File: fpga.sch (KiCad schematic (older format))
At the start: 27 parts, among them IC1 EP4CE10F17, J1 Pinheader_2x5_TH_WALL, U21 EPCS4

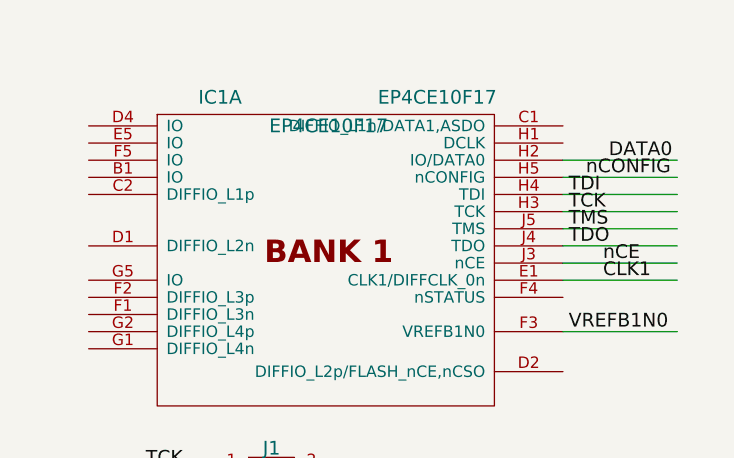
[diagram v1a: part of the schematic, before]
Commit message: Added VCCINT power supply
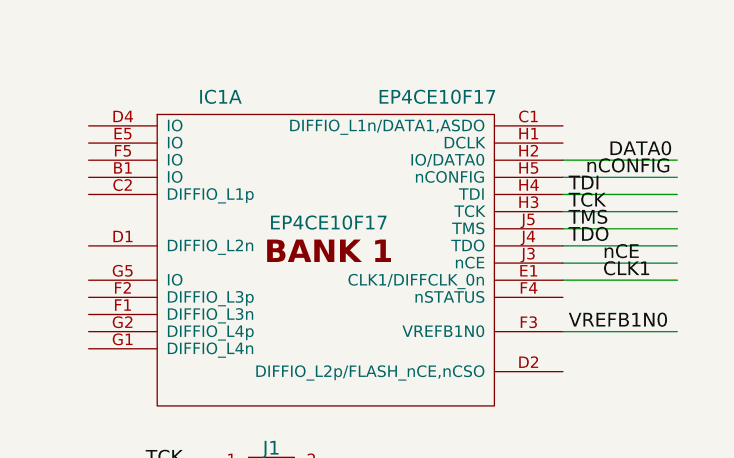
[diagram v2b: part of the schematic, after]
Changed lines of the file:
@@
 EESchema Schematic File Version 2
-LIBS:Sputnik-rescue
 LIBS:sputnik
 LIBS:power
@@
 LIBS:Winbond
 LIBS:Sputnik-cache
-EELAYER 26 0
+EELAYER 25 0
 EELAYER END
 $Descr A3 16535 11693
@@
 P 2600 2125
 F 0 "IC1" H 2125 3400 60  0000 C CNN
-F 1 "EP4CE10F17" H 2600 3275 60  0000 C CNN
+F 1 "EP4CE10F17" H 2600 2850 60  0000 C CNN
 F 2 "lib:BGA-256-NSMD" H 2600 3700 60  0001 C CNN
 F 3 "" H 500 75  60  0000 C CNN
@@
 $EndComp
 $Comp
-L GND #PWR10
+L GND #PWR6
 U 1 1 5807C448
 P 12075 6725
-F 0 "#PWR10" H 12075 6475 50  0001 C CNN
+F 0 "#PWR6" H 12075 6475 50  0001 C CNN
 F 1 "GND" H 12075 6575 50  0000 C CNN
 F 2 "" H 12075 6725 50  0000 C CNN
@@
 $EndComp
 $Comp
-L GND #PWR4
+L GND #PWR5
 U 1 1 57F7A288
 P 2675 3000
-F 0 "#PWR4" H 2675 2750 50  0001 C CNN
+F 0 "#PWR5" H 2675 2750 50  0001 C CNN
 F 1 "GND" H 2675 2850 50  0000 C CNN
 F 2 "" H 2675 3000 50  0000 C CNN
@@
 NoConn ~ 2600 2775
 $Comp
-L +3V3 #PWR2
+L +3V3 #PWR8
 U 1 1 57F8D5C6
 P 13775 2025
-F 0 "#PWR2" H 13875 2075 20  0001 C CNN
+F 0 "#PWR8" H 13875 2075 20  0001 C CNN
 F 1 "+3V3" H 13775 2115 30  0000 C CNN
 F 2 "" H 13775 2025 60  0000 C CNN
@@
 $EndComp
 $Comp
-L GND #PWR3
+L GND #PWR9
 U 1 1 57F8FD8F
 P 13775 2325
-F 0 "#PWR3" H 13775 2075 50  0001 C CNN
+F 0 "#PWR9" H 13775 2075 50  0001 C CNN
 F 1 "GND" H 13775 2175 50  0000 C CNN
 F 2 "" H 13775 2325 50  0000 C CNN
@@
 $EndComp
 $Comp
-L GND #PWR1
+L GND #PWR7
 U 1 1 57F90743
 P 13275 1400
-F 0 "#PWR1" H 13275 1150 50  0001 C CNN
+F 0 "#PWR7" H 13275 1150 50  0001 C CNN
 F 1 "GND" H 13275 1250 50  0000 C CNN
 F 2 "" H 13275 1400 50  0000 C CNN
@@
 $EndComp
 $Comp
-L GND #PWR8
+L GND #PWR2
 U 1 1 58612A86
 P 1700 4125
-F 0 "#PWR8" H 1700 3875 50  0001 C CNN
+F 0 "#PWR2" H 1700 3875 50  0001 C CNN
 F 1 "GND" H 1700 3975 50  0000 C CNN
 F 2 "" H 1700 4125 50  0000 C CNN
@@
 $EndComp
 $Comp
-L +3V3 #PWR5
+L +3V3 #PWR3
 U 1 1 586140D5
 P 2650 3775
-F 0 "#PWR5" H 2750 3825 20  0001 C CNN
+F 0 "#PWR3" H 2750 3825 20  0001 C CNN
 F 1 "+3V3" H 2650 3865 30  0000 C CNN
 F 2 "" H 2650 3775 60  0000 C CNN
@@
 Connection ~ 2650 3825
 $Comp
-L +3V3 #PWR7
+L +3V3 #PWR1
 U 1 1 58614C3F
 P 1575 4025
-F 0 "#PWR7" H 1675 4075 20  0001 C CNN
+F 0 "#PWR1" H 1675 4075 20  0001 C CNN
 F 1 "+3V3" H 1575 4115 30  0000 C CNN
 F 2 "" H 1575 4025 60  0000 C CNN
@@
 $EndComp
 $Comp
-L GND #PWR9
+L GND #PWR4
 U 1 1 586161B6
 P 2650 4500
-F 0 "#PWR9" H 2650 4250 50  0001 C CNN
+F 0 "#PWR4" H 2650 4250 50  0001 C CNN
 F 1 "GND" H 2650 4350 50  0000 C CNN
 F 2 "" H 2650 4500 50  0000 C CNN
@@
 $EndComp
 $Comp
-L GND #PWR6
+L GND #PWR10
 U 1 1 5883481A
 P 14050 3950
-F 0 "#PWR6" H 14050 3700 50  0001 C CNN
+F 0 "#PWR10" H 14050 3700 50  0001 C CNN
 F 1 "GND" H 14050 3800 50  0000 C CNN
 F 2 "" H 14050 3950 50  0000 C CNN

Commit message: Up
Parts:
- added C127: 0,01, Capacitors_SMD:C_0603, symbol C
- added C128: TBD, Capacitors_SMD:C_0603, symbol C
- added Y3: Crystal_GND24, symbol Crystal_GND24
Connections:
- net labels added: CLK50
- net labels removed: CLK1, VCCA2
- wire segments 155 -> 120
- no-connect marks 3 -> 4

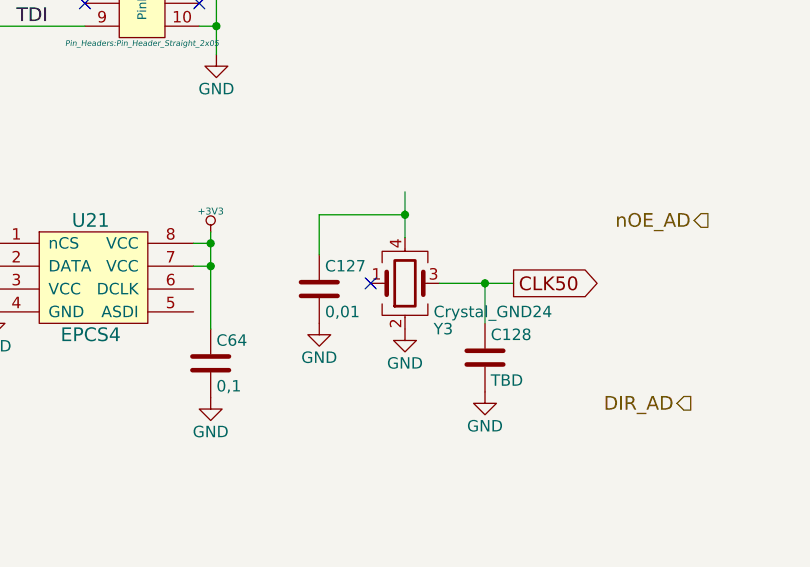
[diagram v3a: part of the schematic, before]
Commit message: Add KXO-V97 footprint
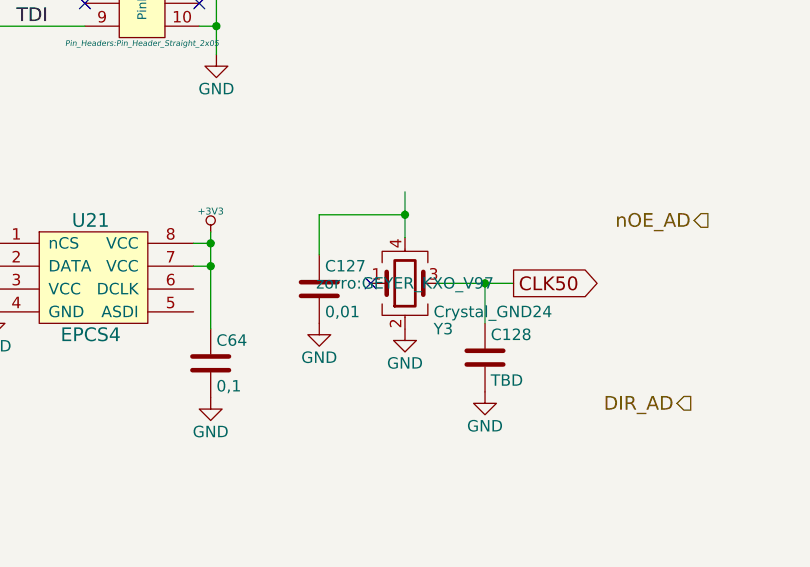
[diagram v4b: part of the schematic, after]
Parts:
- Y3: footprint (none) -> zorro:GEYER_KXO_V97
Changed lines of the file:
@@
 F 0 "Y3" H 3625 4200 50  0000 L CNN
 F 1 "Crystal_GND24" H 3625 4125 50  0000 L CNN
-F 2 "" H 3500 4000 50  0000 C CNN
+F 2 "zorro:GEYER_KXO_V97" H 3500 4000 50  0000 C CNN
 F 3 "" H 3500 4000 50  0000 C CNN
 	1    3500 4000

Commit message: A bit of update
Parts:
- added R34, R35, R36: 10K, Resistors_SMD:R_0603, symbol R_Small
- added R37: 25, Resistors_SMD:R_0603, symbol R_Small
- added R38: 000, Resistors_SMD:R_0603, symbol R_Small
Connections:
- net labels added: ASDO, CONF_DONE, DCLK, nCSO, nSTATUS
- net labels removed: VCCIO1
- wire segments 120 -> 136
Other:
- note added: "ABRACON ASE-50"
- moved on the sheet: C127, C128, Y3

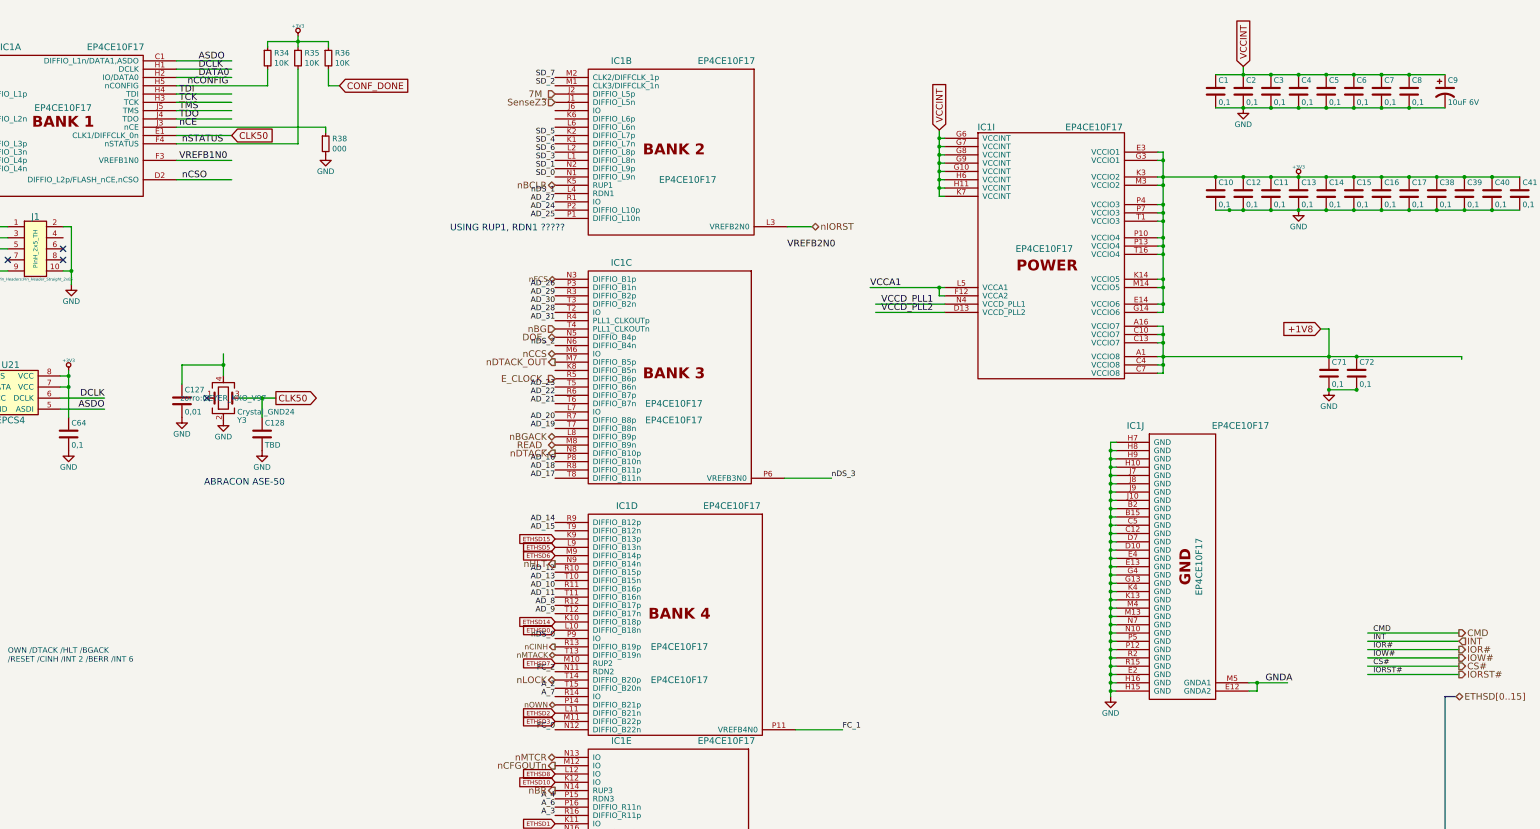
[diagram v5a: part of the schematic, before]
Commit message: VCCA and VCCD_PLL
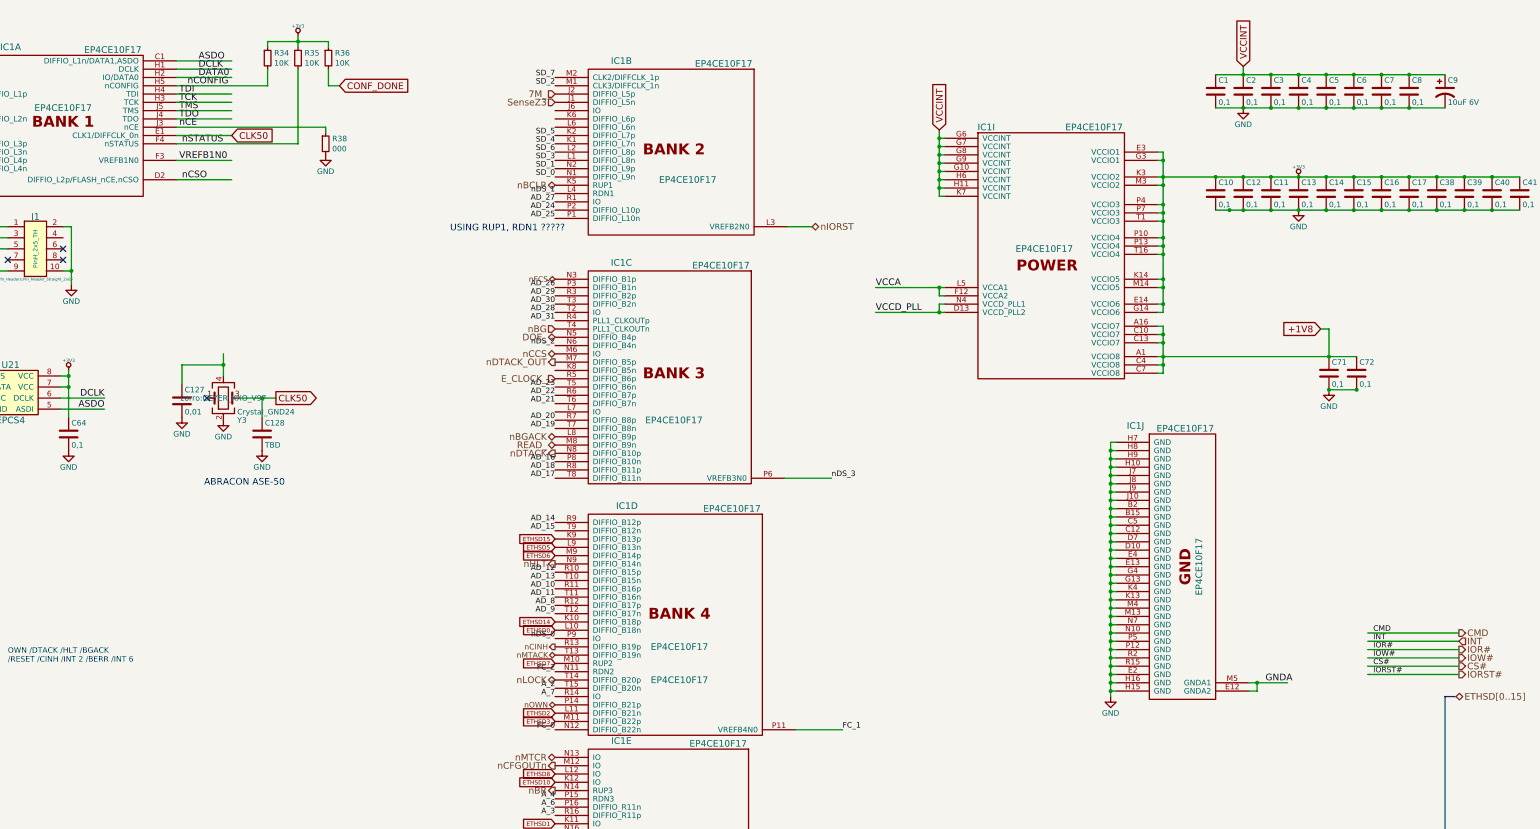
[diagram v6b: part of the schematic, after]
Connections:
- net labels added: VCCA, VCCD_PLL
- net labels removed: VCCA1, VCCD_PLL1, VCCD_PLL2, VREFB2N0
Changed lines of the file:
@@
 F 2 "lib:BGA-256-NSMD" H 2600 3700 60  0001 C CNN
 F 3 "" H 500 75  60  0000 C CNN
-F 4 "EP4CE10F17" H 3075 3400 60  0000 C CNN "Component Value"
+F 4 "EP4CE10F17" H 3050 3375 60  0000 C CNN "Component Value"
 	1    2600 2125
 	1    0    0    -1
@@
 F 2 "lib:BGA-256-NSMD" H 8125 3825 60  0001 C CNN
 F 3 "" H 6025 200 60  0000 C CNN
-F 4 "EP4CE10F17" H 8600 3525 60  0000 C CNN "Component Value"
+F 4 "EP4CE10F17" H 8575 3500 60  0000 C CNN "Component Value"
 	2    8125 2250
 	1    0    0    -1
@@
 F 2 "lib:BGA-256-NSMD" H 8125 5650 60  0001 C CNN
 F 3 "" H 6025 2025 60  0000 C CNN
-F 4 "EP4CE10F17" H 8125 4075 60  0000 C CNN "Component Value"
+F 4 "EP4CE10F17" H 8550 5325 60  0000 C CNN "Component Value"
 	3    8125 4075
 	1    0    0    -1
@@
 F 2 "lib:BGA-256-NSMD" H 12775 7125 60  0001 C CNN
 F 3 "" H 10675 3500 60  0000 C CNN
-F 4 "EP4CE10F17" H 13250 6825 60  0000 C CNN "Component Value"
+F 4 "EP4CE10F17" H 12750 6800 60  0000 C CNN "Component Value"
 	10   12775 5550
 	1    0    0    -1
@@
 Text GLabel 10525 1600 1    60   Input ~ 0
 VCCINT
-Text Label 9900 3025 0    60   ~ 0
-VCCA1
-Text Label 10000 3175 0    60   ~ 0
-VCCD_PLL1
-Text Label 10000 3250 0    60   ~ 0
-VCCD_PLL2
+Text Label 9950 3025 0    60   ~ 0
+VCCA
+Text Label 9950 3250 0    60   ~ 0
+VCCD_PLL
 Text Label 3650 1875 0    60   ~ 0
 VREFB1N0
@@
 F 2 "lib:BGA-256-NSMD" H 8175 7850 60  0001 C CNN
 F 3 "" H 6075 4225 60  0000 C CNN
-F 4 "EP4CE10F17" H 8650 7550 60  0000 C CNN "Component Value"
+F 4 "EP4CE10F17" H 8650 7525 60  0000 C CNN "Component Value"
 	4    8175 6275
 	1    0    0    -1
@@
 	1    0    0    -1
 $EndComp
-Text Label 9150 2675 0    60   ~ 0
-VREFB2N0
 $Comp
 L C C10
@@
 F 2 "lib:BGA-256-NSMD" H 8125 9975 60  0001 C CNN
 F 3 "" H 6025 6350 60  0000 C CNN
-F 4 "EP4CE10F17" H 8600 9675 60  0000 C CNN "Component Value"
+F 4 "EP4CE10F17" H 8525 9650 60  0000 C CNN "Component Value"
 	5    8125 8400
 	1    0    0    -1
@@
 	12550 1875 12500 1875
 Wire Wire Line
-	12500 2100 12550 2100
+	12550 2100 12500 2100
 Wire Wire Line
 	12550 1800 12550 3250
@@
 Connection ~ 12550 3175
 Wire Wire Line
-	12500 3650 15250 3650
+	12500 3650 14300 3650
 Wire Wire Line
 	12550 3525 12500 3525
@@
 Connection ~ 12550 3725
 Wire Wire Line
-	9900 3025 10575 3025
+	9950 3025 10575 3025
 Wire Wire Line
 	10525 3100 10575 3100
 Wire Wire Line
-	10575 3175 9950 3175
-Wire Wire Line
-	10575 3250 9950 3250
+	10575 3175 10525 3175
+Wire Wire Line
+	9950 3250 10575 3250
 Wire Wire Line
 	3625 1125 4125 1125
@@
 	1    0    0    -1
 $EndComp
-Wire Wire Line
-	15250 3650 15250 3675
 Connection ~ 14050 3650
 Text GLabel 13975 3400 0    60   Input ~ 0
@@
 Connection ~ 14050 3950
 Connection ~ 14300 3950
-Connection ~ 14300 3650
 Text HLabel 15100 8275 2    60   BiDi ~ 0
 USBAD[0:15]
@@
 Connection ~ 12550 1875
 $Comp
-L +3V3 #PWR?
+L +3V3 #PWR015
 U 1 1 58AD9DC7
 P 4725 750
-F 0 "#PWR?" H 4825 800 20  0001 C CNN
+F 0 "#PWR015" H 4825 800 20  0001 C CNN
 F 1 "+3V3" H 4725 840 30  0000 C CNN
 F 2 "" H 4725 750 60  0000 C CNN
@@
 	4725 750  4725 850
 Connection ~ 4725 800
+Wire Wire Line
+	10525 3175 10525 3250
+Connection ~ 10525 3250
 $EndSCHEMATC

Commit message: VCCA added
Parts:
- added R45: 000, Resistors_SMD:R_0603, symbol R_Small
- Y3: footprint zorro:GEYER_KXO_V97 -> Crystals:Crystal_SMD_3225-4pin_3.2x2.5mm
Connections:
- net labels added: +2V5
- net labels removed: VCCA
- wire segments 136 -> 139
- no-connect marks 4 -> 3
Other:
- note added: "ABRACON ASE-50 (3.3V)\nASE2 (2.5V)"
- note removed: "ABRACON ASE-50"
- moved on the sheet: C127, C128
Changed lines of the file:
@@
 EESchema Schematic File Version 2
-LIBS:Sputnik-rescue
 LIBS:sputnik
 LIBS:power
@@
 LIBS:Winbond
 LIBS:Sputnik-cache
-EELAYER 26 0
+EELAYER 25 0
 EELAYER END
 $Descr A3 16535 11693
@@
 Text GLabel 10525 1600 1    60   Input ~ 0
 VCCINT
-Text Label 9950 3025 0    60   ~ 0
-VCCA
 Text Label 9950 3250 0    60   ~ 0
 VCCD_PLL
@@
 F 0 "Y3" H 4175 4225 50  0000 L CNN
 F 1 "Crystal_GND24" H 4175 4150 50  0000 L CNN
-F 2 "zorro:GEYER_KXO_V97" H 4050 4025 50  0000 C CNN
+F 2 "Crystals:Crystal_SMD_3225-4pin_3.2x2.5mm" H 4050 4450 50  0000 C CNN
 F 3 "" H 4050 4025 50  0000 C CNN
 	1    4050 4025
@@
 	1    0    0    -1
 $EndComp
-NoConn ~ 3900 4025
-Wire Wire Line
-	4200 4025 4525 4025
-Text GLabel 4525 4025 2    60   Output ~ 0
+Wire Wire Line
+	4200 4025 4825 4025
+Text GLabel 4825 4025 2    60   Output ~ 0
 CLK50
 $Comp
 L C C128
 U 1 1 58A8A4E9
-P 4400 4350
-F 0 "C128" H 4425 4450 50  0000 L CNN
-F 1 "TBD" H 4425 4250 50  0000 L CNN
-F 2 "Capacitors_SMD:C_0603" H 4438 4200 50  0001 C CNN
-F 3 "" H 4400 4350 50  0000 C CNN
-	1    4400 4350
+P 4700 4350
+F 0 "C128" H 4725 4450 50  0000 L CNN
+F 1 "TBD" H 4725 4250 50  0000 L CNN
+F 2 "Capacitors_SMD:C_0603" H 4738 4200 50  0001 C CNN
+F 3 "" H 4700 4350 50  0000 C CNN
+	1    4700 4350
 	1    0    0    -1
 $EndComp
@@
 L C C127
 U 1 1 58A8A576
-P 3675 4050
-F 0 "C127" H 3700 4150 50  0000 L CNN
-F 1 "0,01" H 3700 3950 50  0000 L CNN
-F 2 "Capacitors_SMD:C_0603" H 3713 3900 50  0001 C CNN
-F 3 "" H 3675 4050 50  0000 C CNN
-	1    3675 4050
+P 3425 4050
+F 0 "C127" H 3450 4150 50  0000 L CNN
+F 1 "0,01" H 3450 3950 50  0000 L CNN
+F 2 "Capacitors_SMD:C_0603" H 3463 3900 50  0001 C CNN
+F 3 "" H 3425 4050 50  0000 C CNN
+	1    3425 4050
 	1    0    0    -1
 $EndComp
@@
 L GND #PWR012
 U 1 1 58A8A622
-P 3675 4200
-F 0 "#PWR012" H 3675 3950 50  0001 C CNN
-F 1 "GND" H 3675 4050 50  0000 C CNN
-F 2 "" H 3675 4200 50  0000 C CNN
-F 3 "" H 3675 4200 50  0000 C CNN
-	1    3675 4200
-	1    0    0    -1
-$EndComp
-Wire Wire Line
-	3675 3900 3675 3725
-Wire Wire Line
-	3675 3725 4050 3725
+P 3425 4200
+F 0 "#PWR012" H 3425 3950 50  0001 C CNN
+F 1 "GND" H 3425 4050 50  0000 C CNN
+F 2 "" H 3425 4200 50  0000 C CNN
+F 3 "" H 3425 4200 50  0000 C CNN
+	1    3425 4200
+	1    0    0    -1
+$EndComp
+Wire Wire Line
+	3425 3900 3425 3725
+Wire Wire Line
+	3425 3725 4050 3725
 Wire Wire Line
 	4050 3625 4050 3825
@@
 L GND #PWR013
 U 1 1 58A8A9F2
-P 4400 4500
-F 0 "#PWR013" H 4400 4250 50  0001 C CNN
-F 1 "GND" H 4400 4350 50  0000 C CNN
-F 2 "" H 4400 4500 50  0000 C CNN
-F 3 "" H 4400 4500 50  0000 C CNN
-	1    4400 4500
-	1    0    0    -1
-$EndComp
-Wire Wire Line
-	4400 4200 4400 4025
-Connection ~ 4400 4025
+P 4700 4500
+F 0 "#PWR013" H 4700 4250 50  0001 C CNN
+F 1 "GND" H 4700 4350 50  0000 C CNN
+F 2 "" H 4700 4500 50  0000 C CNN
+F 3 "" H 4700 4500 50  0000 C CNN
+	1    4700 4500
+	1    0    0    -1
+$EndComp
+Wire Wire Line
+	4700 4200 4700 4025
+Connection ~ 4700 4025
 Text GLabel 4125 1650 2    60   Input ~ 0
 CLK50
@@
 Connection ~ 10525 3025
 Text Notes 3875 4825 0    60   ~ 0
-ABRACON ASE-50
+ABRACON ASE-50 (3.3V)\nASE2 (2.5V)
 $Comp
 L R_Small R34
@@
 	10525 3175 10525 3250
 Connection ~ 10525 3250
+$Comp
+L +3V3 #PWR016
+U 1 1 58B48267
+P 3850 3575
+F 0 "#PWR016" H 3950 3625 20  0001 C CNN
+F 1 "+3V3" H 3850 3665 30  0000 C CNN
+F 2 "" H 3850 3575 60  0000 C CNN
+F 3 "" H 3850 3575 60  0000 C CNN
+	1    3850 3575
+	1    0    0    -1
+$EndComp
+$Comp
+L R_Small R45
+U 1 1 58B48E86
+P 3725 3875
+F 0 "R45" H 3784 3921 50  0000 L CNN
+F 1 "000" H 3784 3830 50  0000 L CNN
+F 2 "Resistors_SMD:R_0603" H -725 3075 50  0001 C CNN
+F 3 "" H -725 3075 50  0001 C CNN
+	1    3725 3875
+	1    0    0    -1
+$EndComp
+Wire Wire Line
+	3725 3975 3725 4025
+Wire Wire Line
+	3725 4025 3900 4025
+Wire Wire Line
+	3725 3775 3725 3725
+Connection ~ 3725 3725
+Text GLabel 9950 3025 0    60   Input ~ 12
++2V5
 $EndSCHEMATC
